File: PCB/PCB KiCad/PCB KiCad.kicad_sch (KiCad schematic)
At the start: 0 parts

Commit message: export for review
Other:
- company: (none) -> Plastic Scanner
- title: (none) -> Development Board
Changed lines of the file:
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@@
 (kicad_sch (version 20211123) (generator eeschema)
   (paper "A4")
+  (title_block
+    (title "Development Board")
+    (date "2022-03-15")
+    (rev "2.1")
+    (company "Plastic Scanner")
+  )
   (bus (pts (xy 168.275 92.075) (xy 175.895 92.075))
     (stroke (width 0) (type default) (color 0 0 0 0))

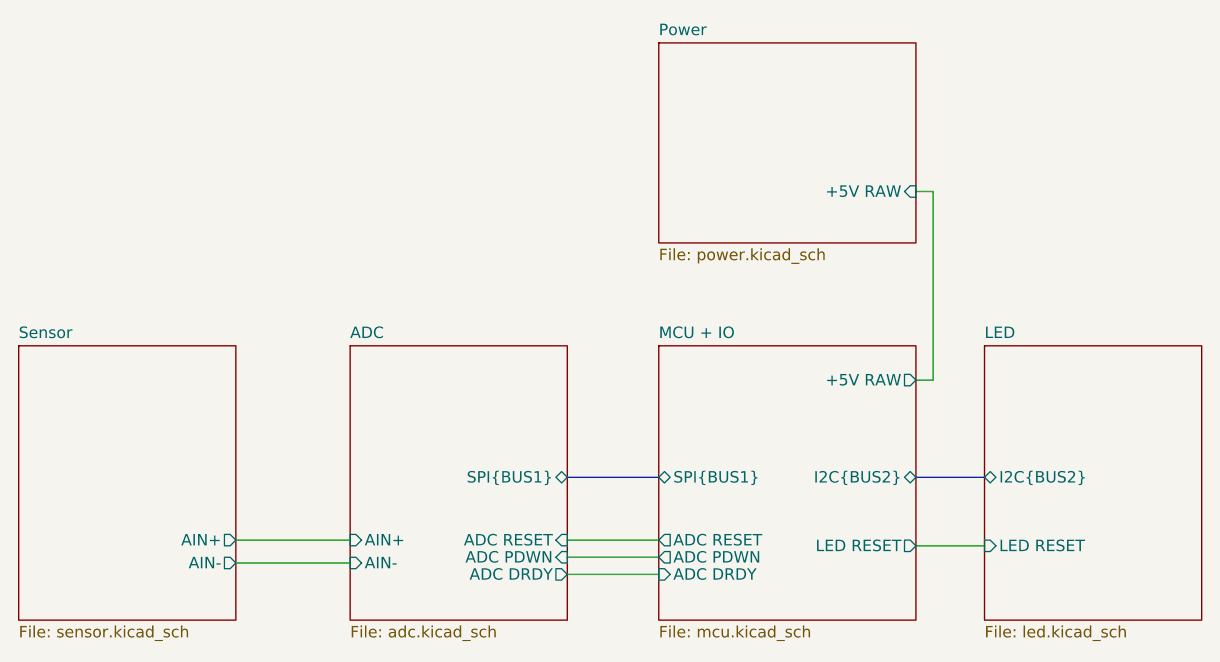
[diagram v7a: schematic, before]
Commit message: v2.2.0 first attempt for new ICs
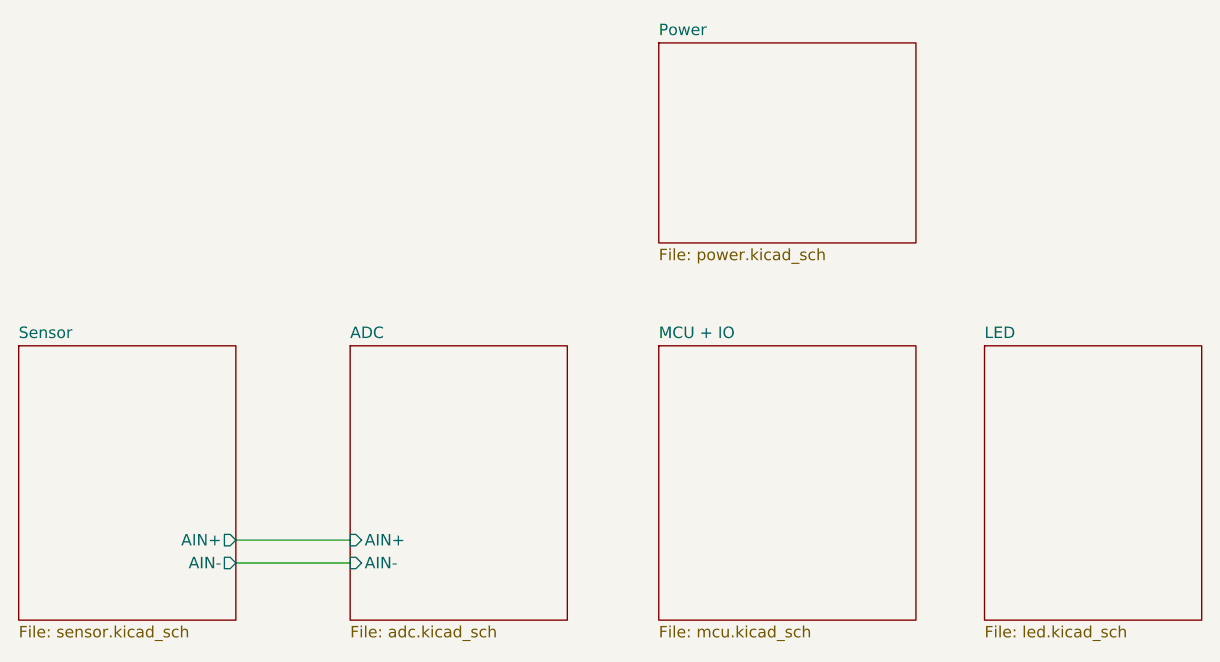
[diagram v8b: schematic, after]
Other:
- sheet ADC ports: added none; removed ADC DRDY, ADC PDWN, ADC RESET, SPI{BUS1}
- sheet LED ports: added none; removed I2C{BUS2}, LED RESET
- sheet MCU + IO ports: added none; removed +5V RAW, ADC DRDY, ADC PDWN, ADC RESET, I2C{BUS2}, LED RESET, SPI{BUS1}
- sheet Power ports: added none; removed +5V RAW
